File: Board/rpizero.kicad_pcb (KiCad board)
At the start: 4 copper layers, 30 x 64 mm, 68 parts, among them J3 FJ, J4 FJ, J5 FJ, J6 FJ, P1 CONN_01X03, P10 CONN_01X03, P2 CONN_01X03, P3 CONN_01X03, P4 CONN_01X03, P5 CONN_01X03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

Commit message: Bazeline documents: rpi2HAT.sch rpiHATv2.net zero+.kicad.pcb
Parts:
- removed 5-15out1: CONN_01X02, Pin_Headers:Pin_Header_Straight_1x02
- removed Buck1: CONN_01X03, Pin_Headers:Pin_Header_Straight_1x03
- removed C7: C, Capacitors_SMD:C_0805
- added 5-15in1: CONN_01X02, Pin_Headers:Pin_Header_Straight_1x02, F.Cu at (213.5, 140.5)
- added 5out1: CONN_01X02, Pin_Headers:Pin_Header_Straight_1x02, F.Cu at (208.0, 132.8)
- added C5: C, Capacitors_SMD:C_0805, F.Cu at (211.7, 94.3)
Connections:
- C21 pad 1: /GND-SERVO -> Net-(C21-Pad1)
- C3 pad 1: /GND-SERVO -> Net-(C21-Pad1)
- C4 pad 1: /GND-SERVO -> Net-(C21-Pad1)
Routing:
- net /GND-SERVO: track 34.4 -> 75.1 mm, vias 11 -> 17
- net /+5-SERVO: track 102.3 -> 120.0 mm, vias 5 -> 7
- net Net-(C21-Pad1): track 0.00 -> 12.8 mm, vias 0 -> 2

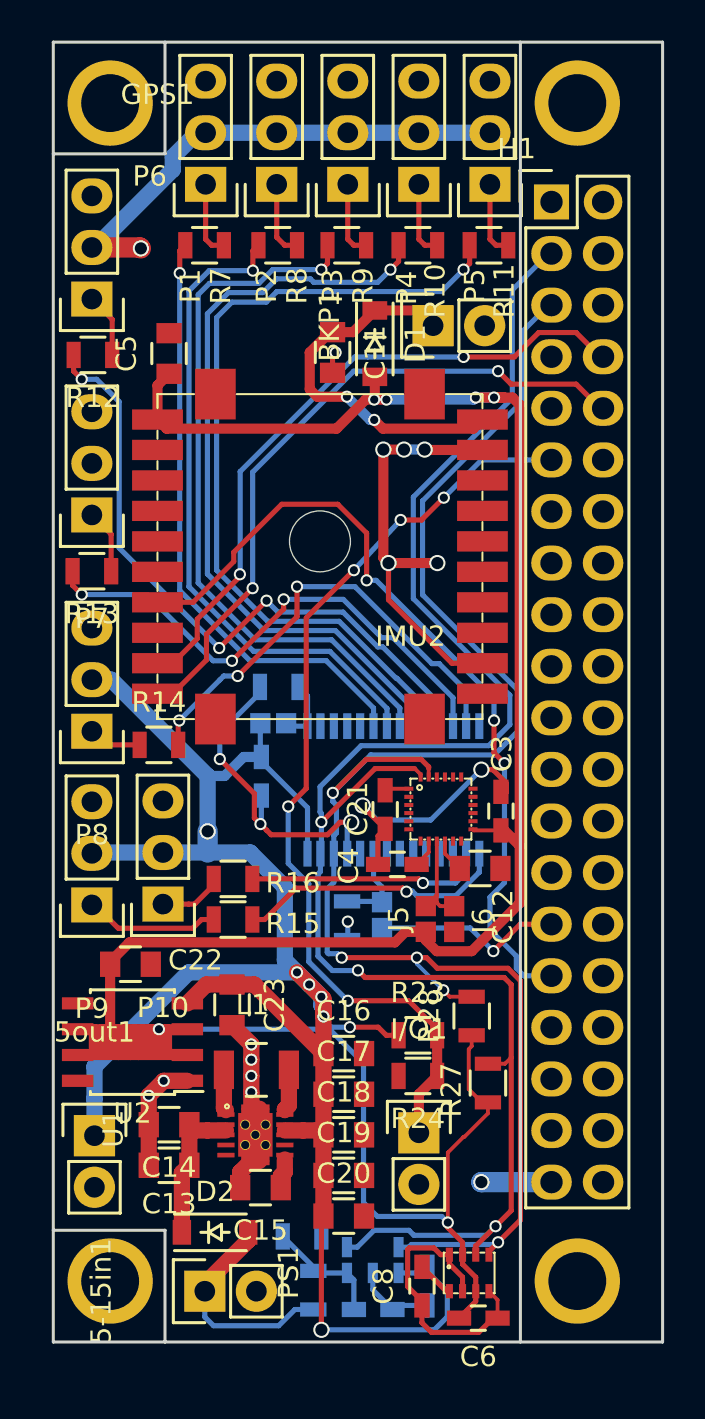
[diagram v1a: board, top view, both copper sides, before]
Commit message: Added zones for buc/boost converter. changed pad filling
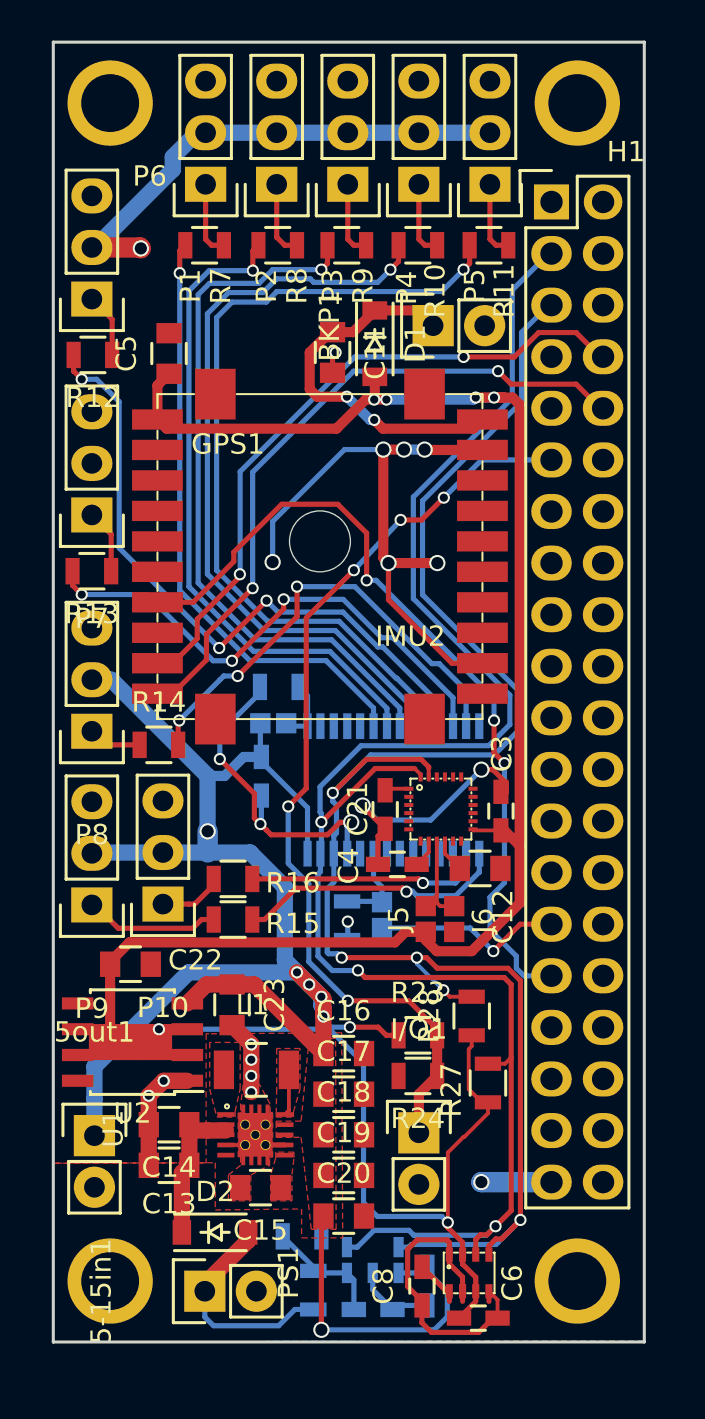
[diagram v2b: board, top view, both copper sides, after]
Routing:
- net /+5-SERVO: track 120.0 -> 109.5 mm
- net /GND-SERVO: track 75.1 -> 83.0 mm, vias 17 -> 18
- net Net-(L1-Pad1): track 2.44 -> 0.00 mm
- net /RPI-SCL: track 83.2 -> 85.0 mm
- net Net-(C15-Pad1): track 1.68 -> 0.00 mm
- net Net-(C8-Pad2): track 1.85 -> 2.35 mm
- added copper zone on F.Cu, net /+5-SERVO
- added copper zone on F.Cu, net Net-(C15-Pad1)
- added copper zone on F.Cu, net Net-(L1-Pad1)
- added copper zone on F.Cu, net Net-(L1-Pad2)
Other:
- board size 30 x 64 mm -> 29.1 x 64 mm

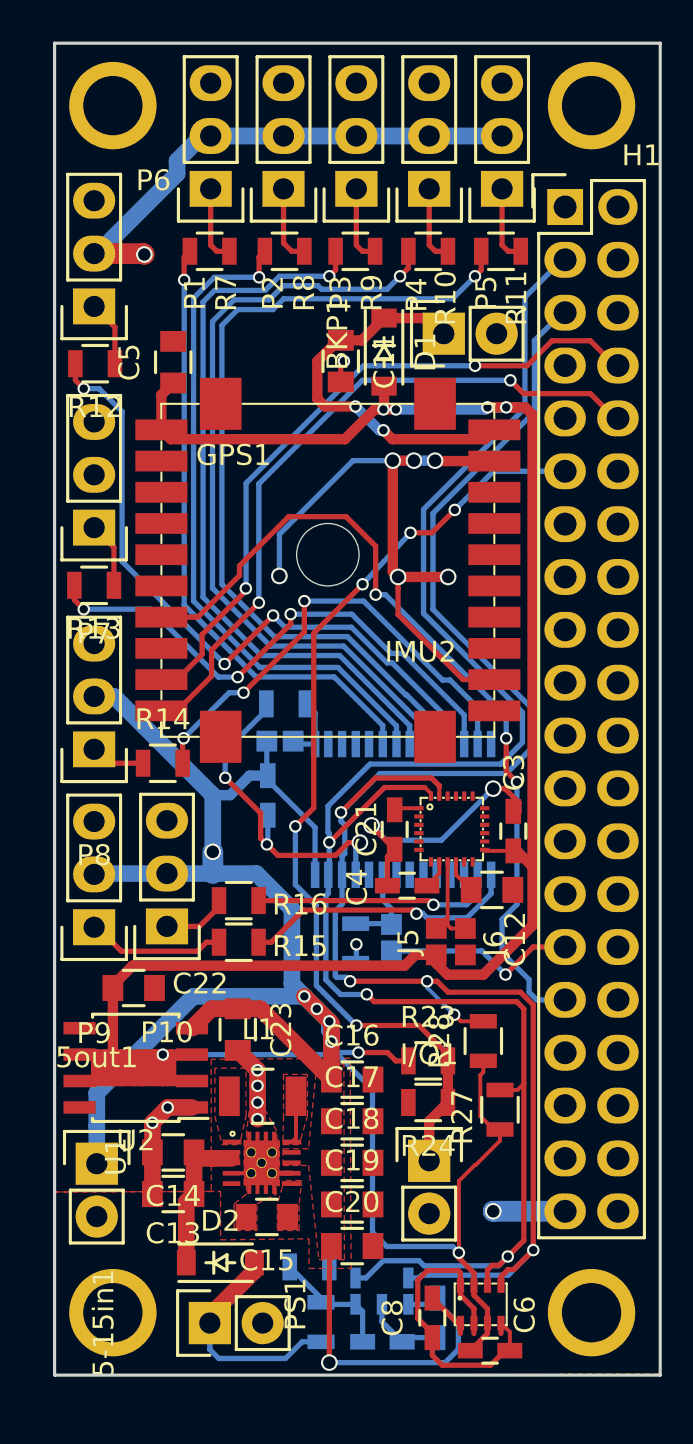
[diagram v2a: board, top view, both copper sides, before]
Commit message: corrected clereance in zones, fixed some grounding issues
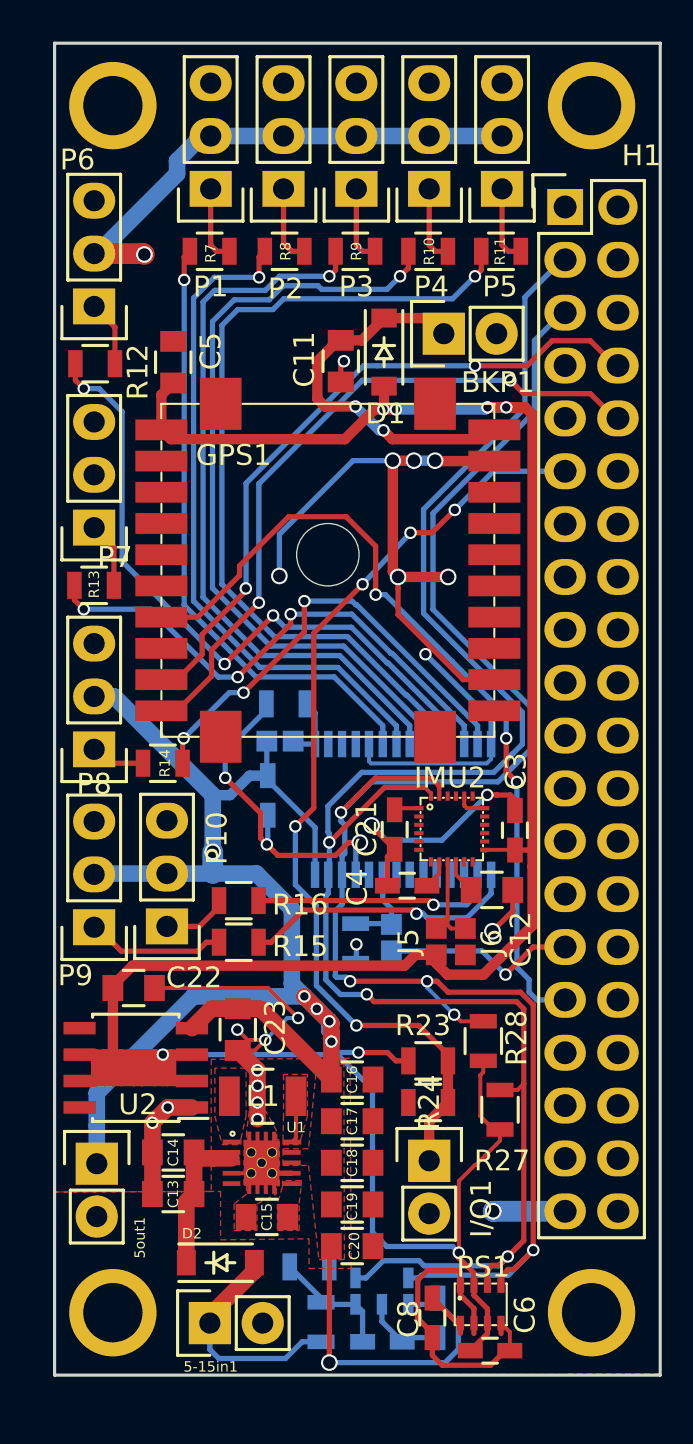
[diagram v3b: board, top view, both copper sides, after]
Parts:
- moved C3 0.09 mm to (228.1, 116.8)
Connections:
- GPS1 pad : (no net) -> /GND-SERVO
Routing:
- net /GND-SERVO: track 83.0 -> 112.8 mm, vias 18 -> 23
- net Net-(C21-Pad1): track 12.8 -> 12.2 mm
- net /RPI-GPIO6: track 40.4 -> 39.8 mm
- net Net-(IMU1-Pad13): track 22.8 -> 22.3 mm
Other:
- copper layers 4 -> 2

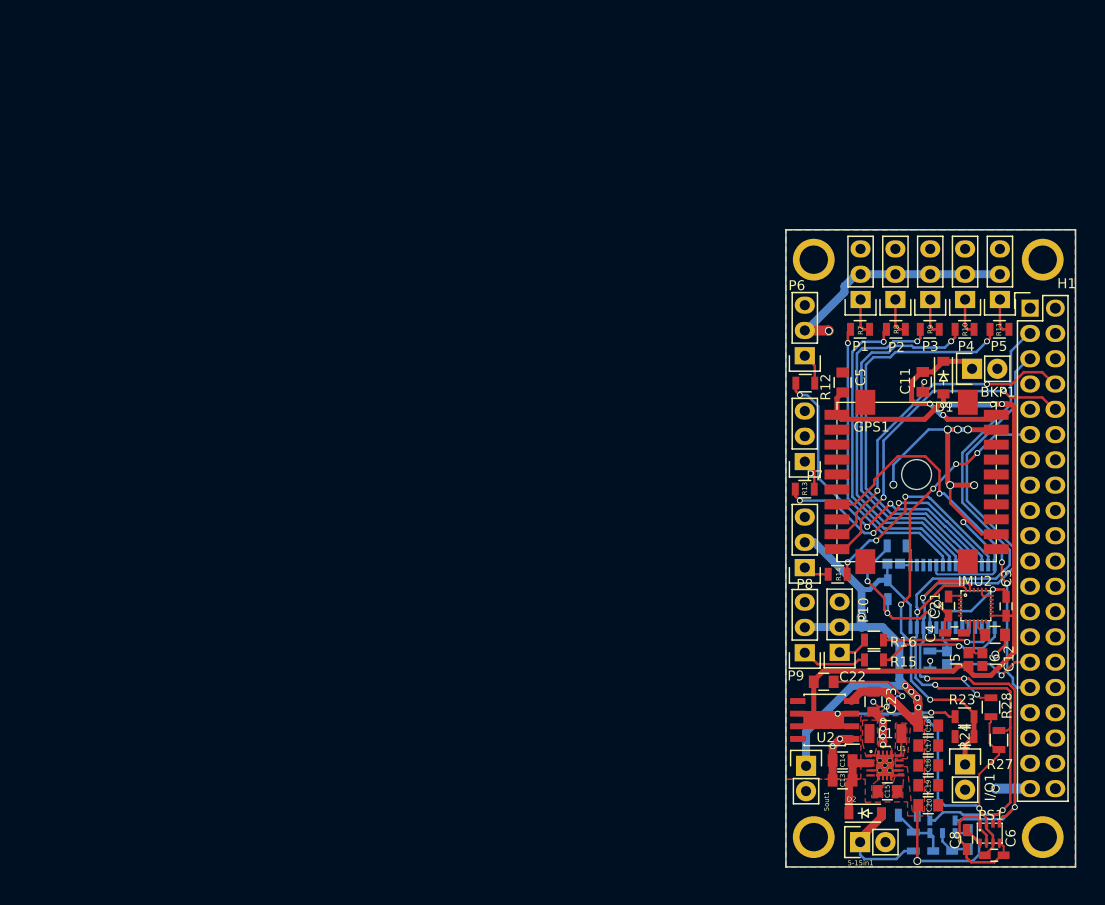
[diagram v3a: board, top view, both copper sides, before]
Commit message: Minor placement addjustment.
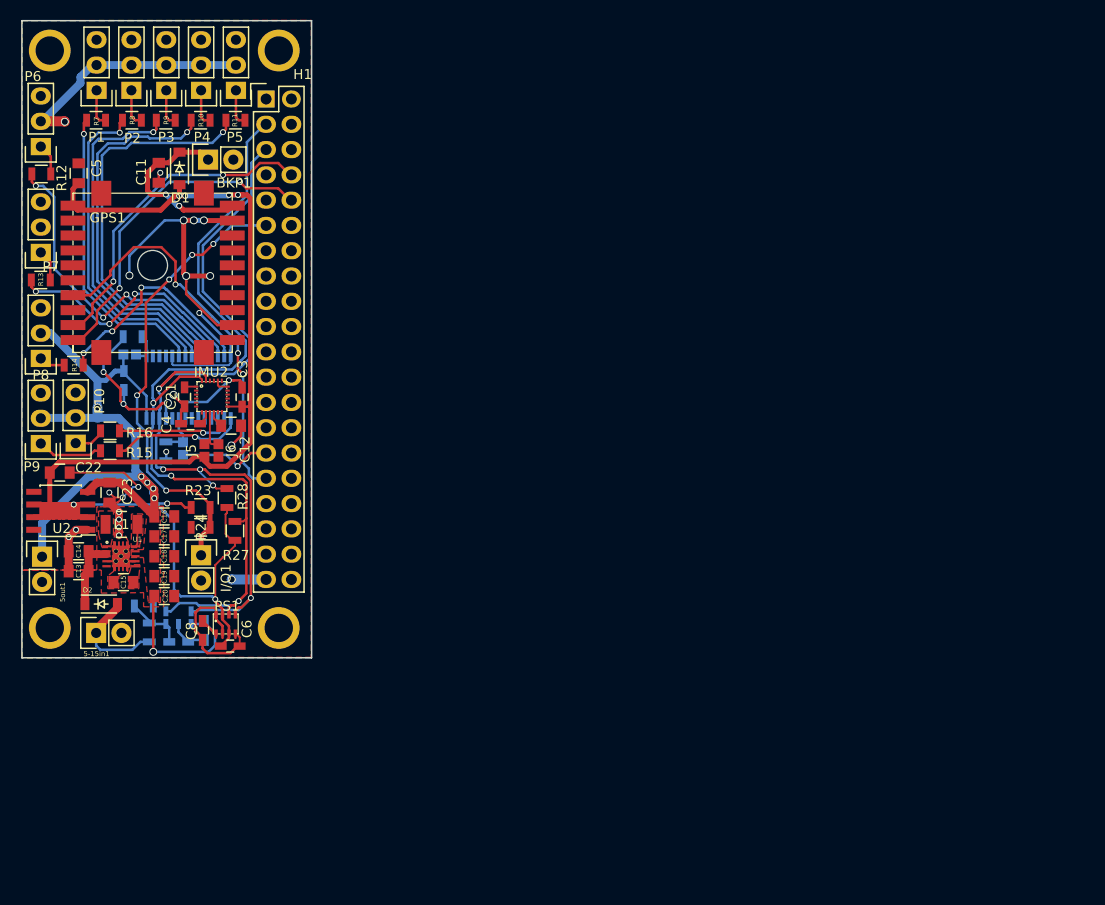
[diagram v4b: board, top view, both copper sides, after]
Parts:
- moved 5-15in1 79.6 mm to (136.7, 119.5)
- moved 5out1 79.6 mm to (131.3, 111.8)
- moved ADC1 79.6 mm to (146.3, 118.6)
- moved C1 79.6 mm to (145.0, 120.4)
- moved C10 79.6 mm to (139.5, 94.1)
- moved C11 79.6 mm to (143.0, 73.3)
- moved C16 79.6 mm to (143.6, 107.8)
- moved C17 79.6 mm to (143.6, 109.8)
- moved C18 79.6 mm to (143.6, 111.8)
- moved C19 79.6 mm to (143.6, 113.8)
- moved C20 79.6 mm to (143.6, 115.8)
- moved C21 79.6 mm to (145.6, 95.8)
- moved C22 79.6 mm to (133.1, 103.4)
- moved C23 79.6 mm to (138.1, 105.4)
- moved C3 79.6 mm to (151.4, 95.8)
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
